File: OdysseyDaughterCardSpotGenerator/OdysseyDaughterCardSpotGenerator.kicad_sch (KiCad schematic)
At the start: 22 parts

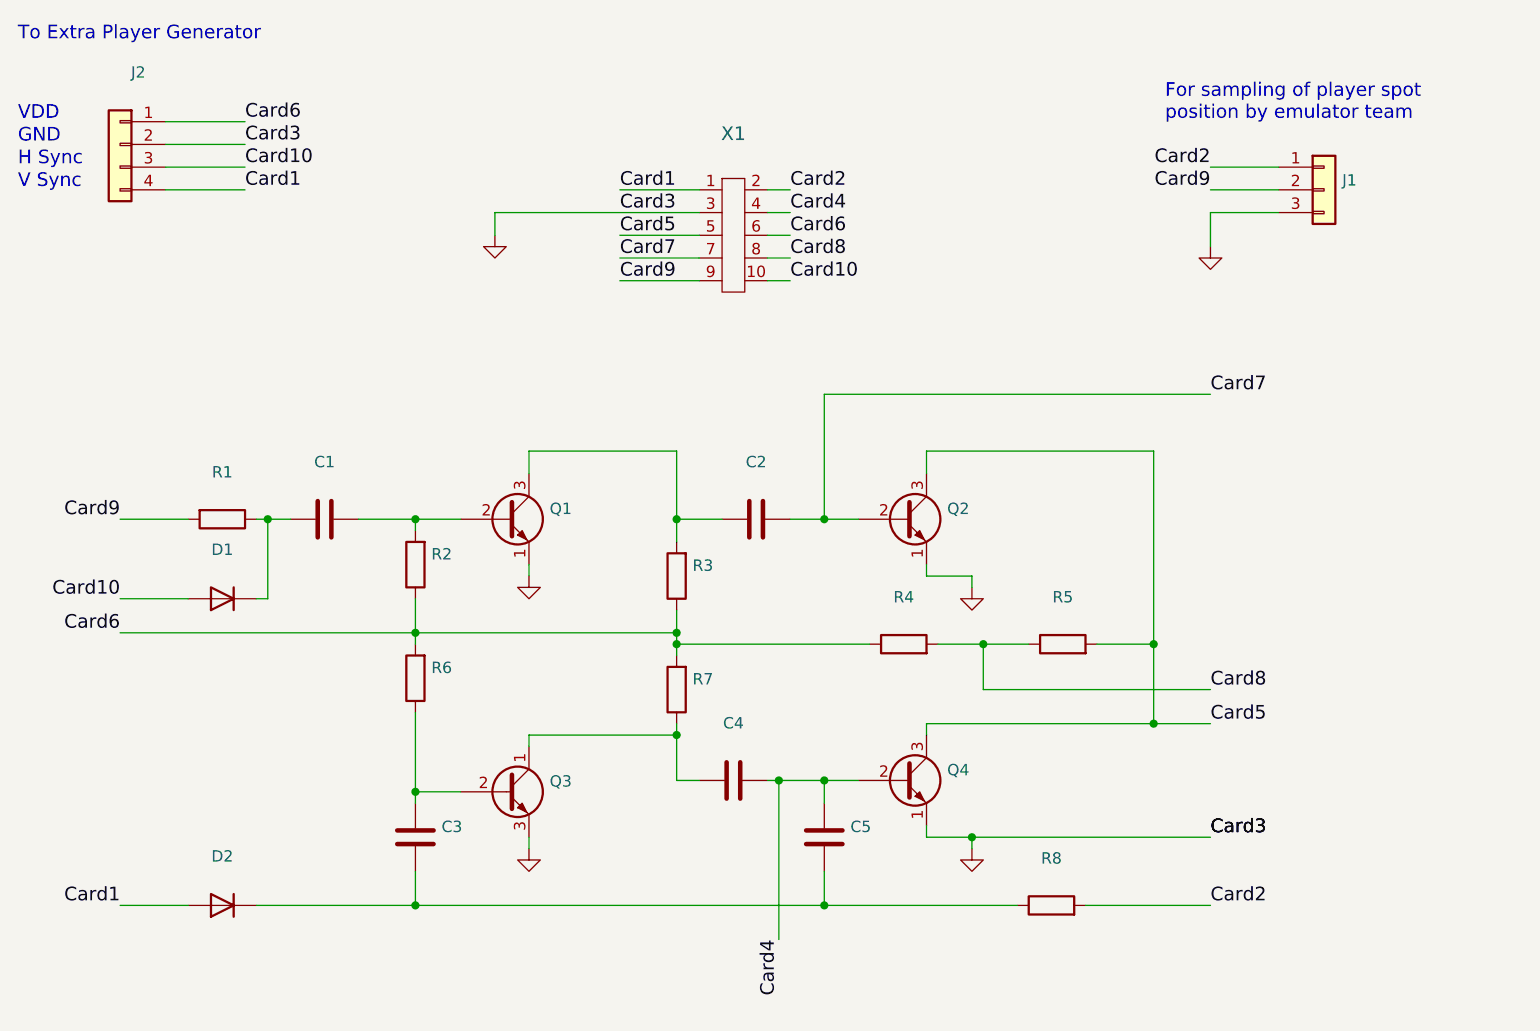
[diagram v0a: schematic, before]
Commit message: OdysseyDaughterCardSpotGenerator wider transistor footprint, add logo, generate pdf, images, 3d models
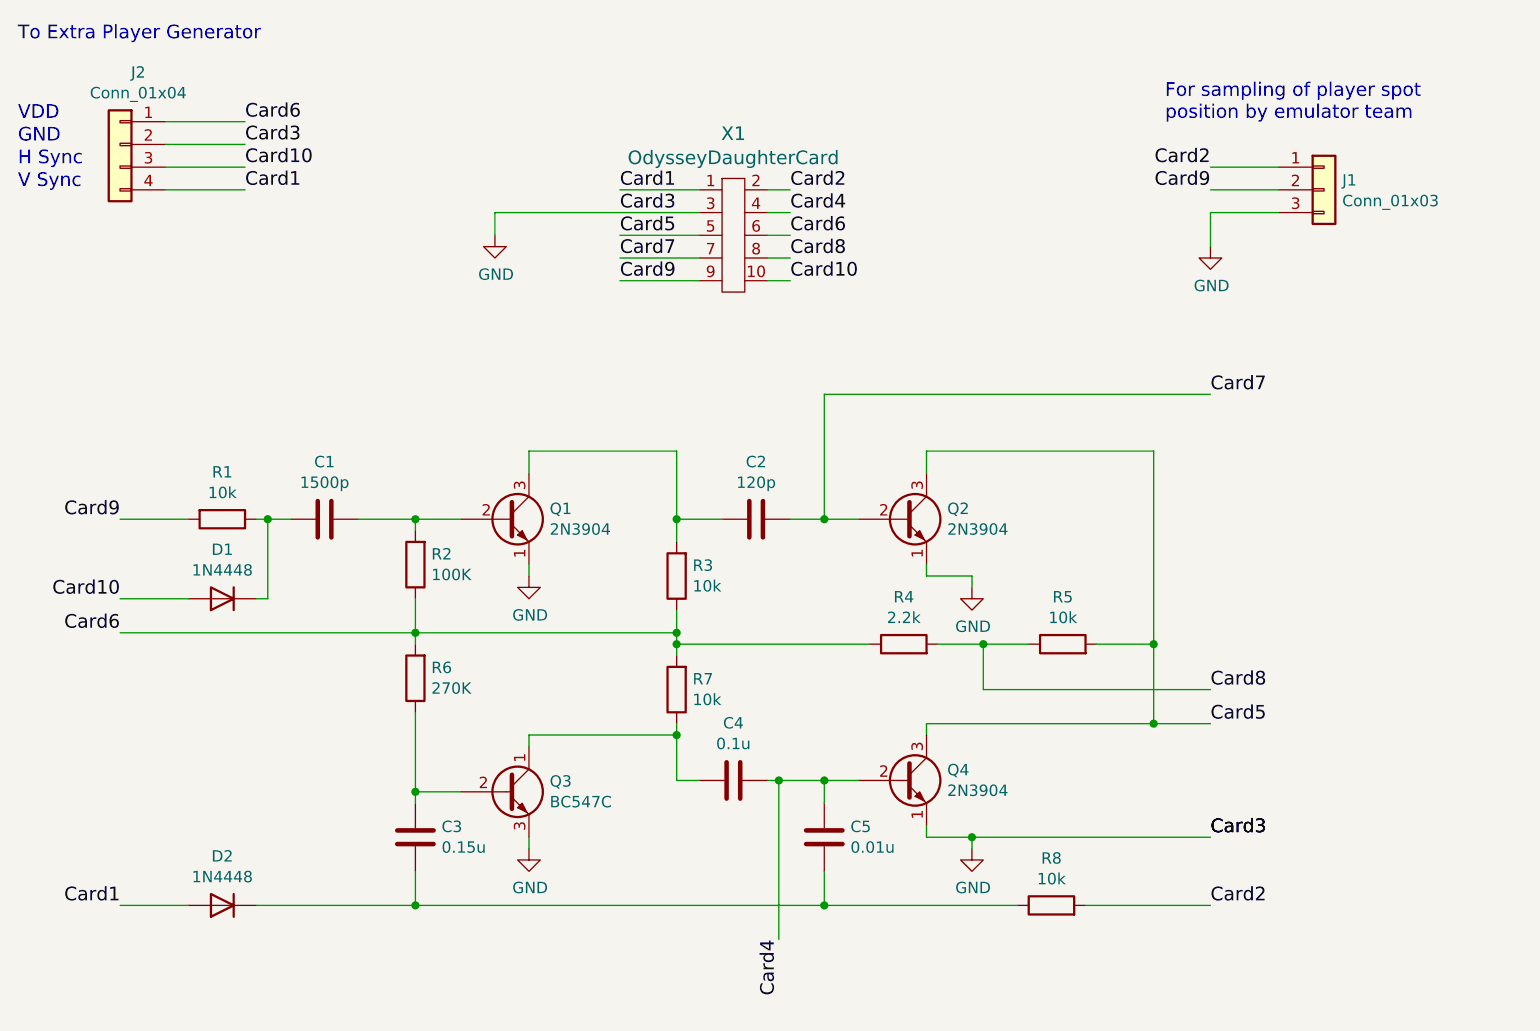
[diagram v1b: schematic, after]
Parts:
- C1: value (none) -> 1500p; footprint (none) -> Capacitor_THT:C_Rect_L4.0mm_W2.5mm_P2.50mm
- C2: value (none) -> 120p; footprint (none) -> Capacitor_THT:C_Rect_L4.0mm_W2.5mm_P2.50mm
- C3: value (none) -> 0.15u; footprint (none) -> Capacitor_THT:C_Rect_L4.6mm_W5.5mm_P2.50mm_MKS02_FKP02
- C4: value (none) -> 0.1u; footprint (none) -> Capacitor_THT:C_Rect_L4.0mm_W2.5mm_P2.50mm
- C5: value (none) -> 0.01u; footprint (none) -> Capacitor_THT:C_Rect_L4.0mm_W2.5mm_P2.50mm
- D1, D2: value (none) -> 1N4448; footprint (none) -> Diode_THT:D_DO-35_SOD27_P7.62mm_Horizontal
- J1: value (none) -> Conn_01x03; footprint (none) -> Connector_PinHeader_2.54mm:PinHeader_1x03_P2.54mm_Vertical
- J2: value (none) -> Conn_01x04; footprint (none) -> Connector_PinHeader_2.54mm:PinHeader_1x04_P2.54mm_Vertical
- Q1, Q2, Q4: value (none) -> 2N3904; footprint (none) -> Package_TO_SOT_THT:TO-92_Inline_Wide
- Q3: value (none) -> BC547C; footprint (none) -> Package_TO_SOT_THT:TO-92_Inline_Wide
- R1, R3, R5, R7, R8: value (none) -> 10k; footprint (none) -> Resistor_THT:R_Axial_DIN0207_L6.3mm_D2.5mm_P7.62mm_Horizontal
- R2: value (none) -> 100K; footprint (none) -> Resistor_THT:R_Axial_DIN0207_L6.3mm_D2.5mm_P7.62mm_Horizontal
- R4: value (none) -> 2.2k; footprint (none) -> Resistor_THT:R_Axial_DIN0207_L6.3mm_D2.5mm_P7.62mm_Horizontal
- R6: value (none) -> 270K; footprint (none) -> Resistor_THT:R_Axial_DIN0207_L6.3mm_D2.5mm_P7.62mm_Horizontal
- X1: value (none) -> OdysseyDaughterCard; footprint (none) -> Odyssey_Daughter_Card:Odyssey_Daughter_Card
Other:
- company: University of Pittsburgh - Odyssey Restoration Project -> University of Pittsburgh - OdysseyNow
